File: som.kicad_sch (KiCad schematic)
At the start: 33 parts, among them M1 jetson-orin-nx/nano-module, U1 74LVC1T45GM

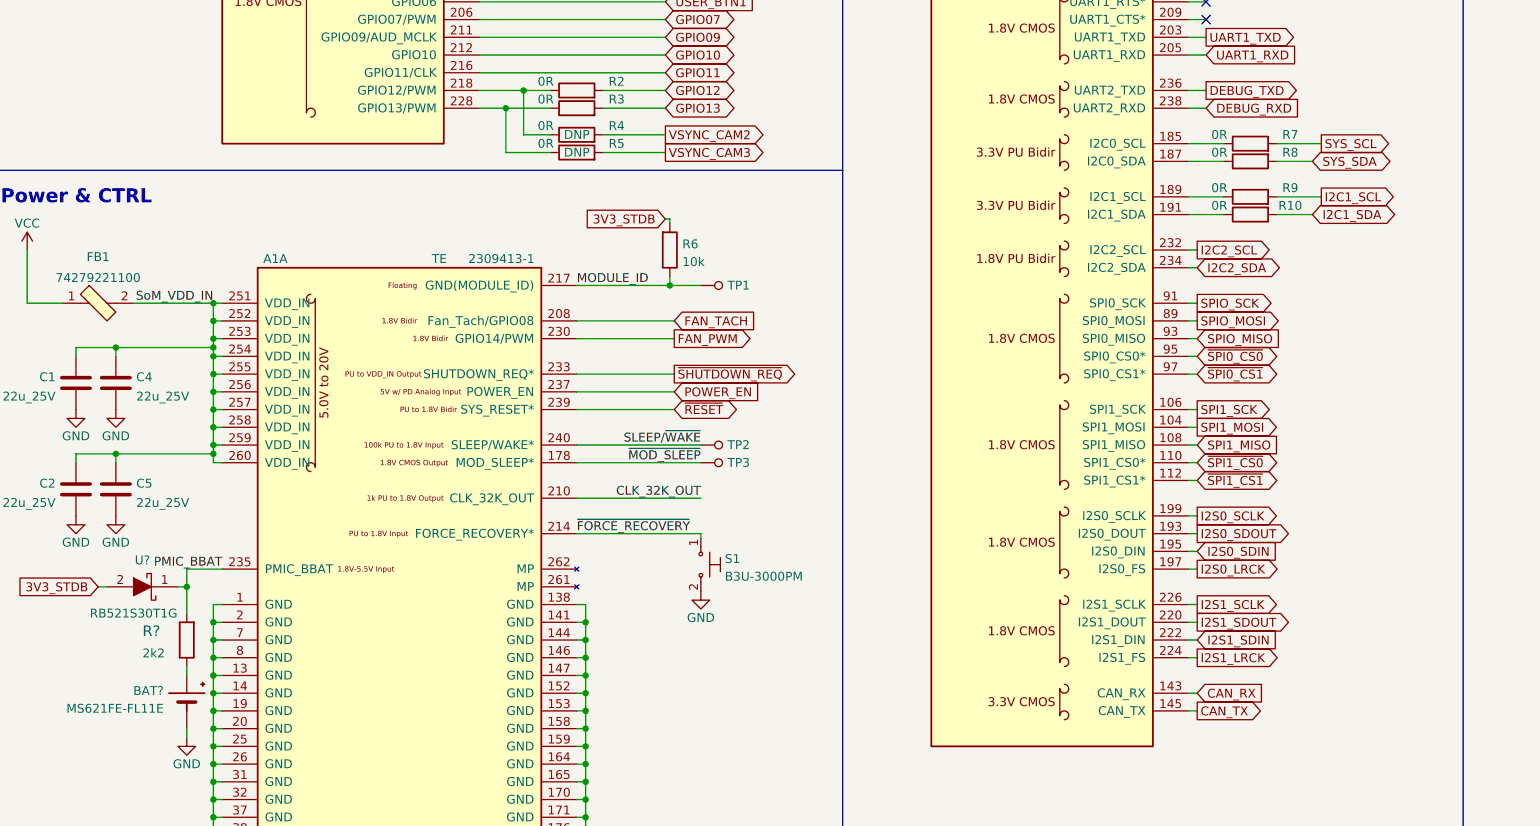
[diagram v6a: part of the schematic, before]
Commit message: Remove 0Rs from I2C pins near SoM
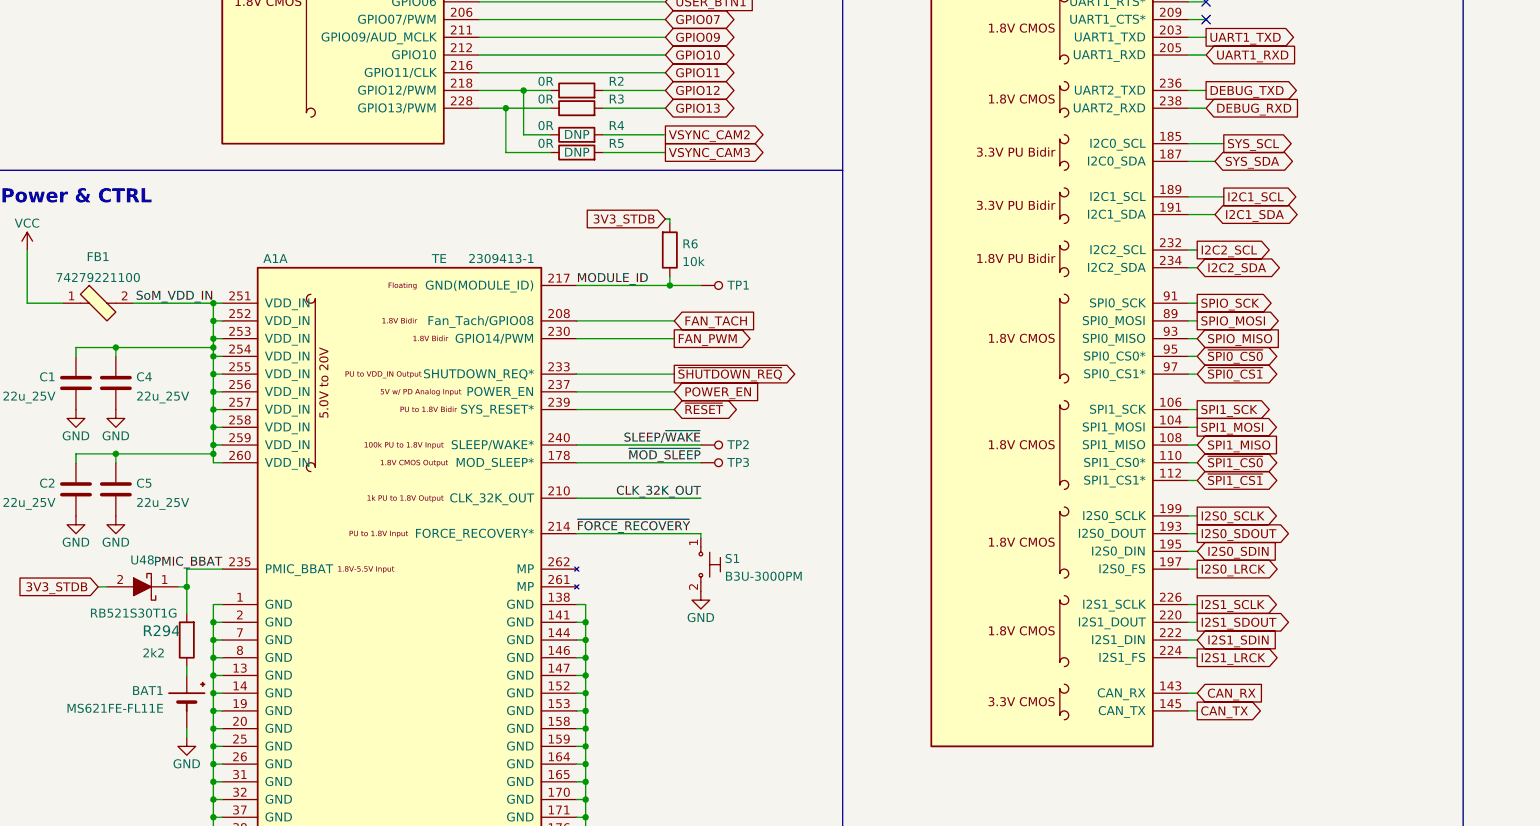
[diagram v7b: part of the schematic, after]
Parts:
- removed R10, R7, R8, R9: R_0R_0402, antmicro-footprints:0402-res, symbol antmicroResistors0402:R_0R_0402
- gave numbers to parts that had none: 3
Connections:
- net I2C1_SCL: now also A1.189 (I2C1_SCL)
- net I2C1_SDA: now also A1.191 (I2C1_SDA)
- net SYS_SCL: now also A1.185 (I2C0_SCL)
- net SYS_SDA: now also A1.187 (I2C0_SDA)
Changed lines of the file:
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@@
     (stroke (width 0) (type default) (color 0 0 0 0))
   )
-  (wire (pts (xy 207.01 73.66) (xy 201.93 73.66))
-    (stroke (width 0) (type default) (color 0 0 0 0))
-  )
   (wire (pts (xy 45.72 138.43) (xy 45.72 139.7))
     (stroke (width 0) (type default) (color 0 0 0 0))
@@
     (stroke (width 0) (type default) (color 0 0 0 0))
   )
-  (wire (pts (xy 194.31 66.04) (xy 189.23 66.04))
+  (wire (pts (xy 193.04 66.04) (xy 189.23 66.04))
     (stroke (width 0) (type default) (color 0 0 0 0))
   )
@@
     (stroke (width 0) (type default) (color 0 0 0 0))
   )
-  (wire (pts (xy 189.23 73.66) (xy 194.31 73.66))
+  (wire (pts (xy 189.23 73.66) (xy 193.04 73.66))
     (stroke (width 0) (type default) (color 0 0 0 0))
   )
@@
     (stroke (width 0) (type default) (color 0 0 0 0))
   )
-  (wire (pts (xy 208.28 63.5) (xy 201.93 63.5))
-    (stroke (width 0) (type default) (color 0 0 0 0))
-  )
   (wire (pts (xy 119.38 109.22) (xy 101.6 109.22))
     (stroke (width 0) (type default) (color 0 0 0 0))
@@
     (stroke (width 0) (type default) (color 0 0 0 0))
   )
-  (wire (pts (xy 207.01 66.04) (xy 201.93 66.04))
-    (stroke (width 0) (type default) (color 0 0 0 0))
-  )
   (wire (pts (xy 278.13 101.6) (xy 296.545 101.6))
     (stroke (width 0) (type default) (color 0 0 0 0))
@@
     (stroke (width 0) (type default) (color 0 0 0 0))
   )
-  (wire (pts (xy 194.31 63.5) (xy 189.23 63.5))
+  (wire (pts (xy 189.23 63.5) (xy 194.31 63.5))
     (stroke (width 0) (type default) (color 0 0 0 0))
   )
@@
     (stroke (width 0) (type default) (color 0 0 0 0))
   )
-  (wire (pts (xy 208.28 71.12) (xy 201.93 71.12))
-    (stroke (width 0) (type default) (color 0 0 0 0))
-  )
   (wire (pts (xy 190.5 93.98) (xy 189.23 93.98))
     (stroke (width 0) (type default) (color 0 0 0 0))
@@
     )
   )
-  (global_label "I2C1_SDA" (shape bidirectional) (at 207.01 73.66 0)
+  (global_label "I2C1_SDA" (shape bidirectional) (at 193.04 73.66 0)
     (effects (font (size 1.27 1.27)) (justify left))
-    (property "Intersheet References" "${INTERSHEET_REFS}" (id 0) (at 219.71 73.66 0)
+    (property "Intersheet References" "${INTERSHEET_REFS}" (id 0) (at 205.74 73.66 0)
       (effects (font (size 1.27 1.27)) (justify left))
     )
@@
     )
   )
-  (global_label "SYS_SDA" (shape bidirectional) (at 207.01 66.04 0)
+  (global_label "SYS_SDA" (shape bidirectional) (at 193.04 66.04 0)
     (effects (font (size 1.27 1.27)) (justify left))
-    (property "Intersheet References" "${INTERSHEET_REFS}" (id 0) (at 219.71 66.04 0)
+    (property "Intersheet References" "${INTERSHEET_REFS}" (id 0) (at 205.74 66.04 0)
       (effects (font (size 1.27 1.27)) (justify left))
     )
@@
     )
   )
-  (global_label "SYS_SCL" (shape output) (at 208.28 63.5 0)
+  (global_label "SYS_SCL" (shape output) (at 194.31 63.5 0)
     (effects (font (size 1.27 1.27)) (justify left))
-    (property "Intersheet References" "${INTERSHEET_REFS}" (id 0) (at 219.71 63.5 0)
+    (property "Intersheet References" "${INTERSHEET_REFS}" (id 0) (at 205.74 63.5 0)
       (effects (font (size 1.27 1.27)) (justify left))
     )
@@
     )
   )
-  (global_label "I2C1_SCL" (shape output) (at 208.28 71.12 0)
+  (global_label "I2C1_SCL" (shape output) (at 194.31 71.12 0)
     (effects (font (size 1.27 1.27)) (justify left))
-    (property "Intersheet References" "${INTERSHEET_REFS}" (id 0) (at 219.71 71.12 0)
+    (property "Intersheet References" "${INTERSHEET_REFS}" (id 0) (at 205.74 71.12 0)
       (effects (font (size 1.27 1.27)) (justify left))
     )
@@
     )
   )
-  (symbol (lib_id "antmicroResistors0402:R_0R_0402") (at 198.12 63.5 0) (unit 1)
-    (in_bom yes) (on_board yes)
-    (property "Reference" "R7" (id 0) (at 203.835 62.23 0))
-    (property "Value" "R_0R_0402" (id 1) (at 198.12 67.31 0)
-      (effects (font (size 1.27 1.27)) hide)
-    )
-    (property "Footprint" "antmicro-footprints:0402-res" (id 2) (at 203.2 58.42 0)
-      (effects (font (size 1.524 1.524)) (justify left) hide)
-    )
-    (property "Datasheet" "" (id 3) (at 198.12 63.5 0)
-      (effects (font (size 1.27 1.27)) hide)
-    )
-    (property "Manufacturer" "PANASONIC" (id 4) (at 203.2 53.34 0)
-      (effects (font (size 1.524 1.524)) (justify left) hide)
-    )
-    (property "MPN" "ERJ2GE0R00X" (id 5) (at 203.2 55.88 0)
-      (effects (font (size 1.524 1.524)) (justify left) hide)
-    )
-    (property "Val" "0R" (id 6) (at 193.675 62.23 0))
-    (pin "1")
-    (pin "2")
-  )
   (symbol (lib_id "power:+1V8") (at 24.765 237.49 0) (unit 1)
     (in_bom yes) (on_board yes)
@@
     (pin "1")
   )
-  (symbol (lib_id "antmicroResistors0402:R_0R_0402") (at 198.12 73.66 0) (mirror x) (unit 1)
-    (in_bom yes) (on_board yes)
-    (property "Reference" "R10" (id 0) (at 203.835 72.39 0))
-    (property "Value" "R_0R_0402" (id 1) (at 198.12 69.85 0)
-      (effects (font (size 1.27 1.27)) hide)
-    )
-    (property "Footprint" "antmicro-footprints:0402-res" (id 2) (at 203.2 78.74 0)
-      (effects (font (size 1.524 1.524)) (justify left) hide)
-    )
-    (property "Datasheet" "" (id 3) (at 198.12 73.66 0)
-      (effects (font (size 1.27 1.27)) hide)
-    )
-    (property "Manufacturer" "PANASONIC" (id 4) (at 203.2 83.82 0)
-      (effects (font (size 1.524 1.524)) (justify left) hide)
-    )
-    (property "MPN" "ERJ2GE0R00X" (id 5) (at 203.2 81.28 0)
-      (effects (font (size 1.524 1.524)) (justify left) hide)
-    )
-    (property "Val" "0R" (id 6) (at 193.675 72.39 0))
-    (pin "1")
-    (pin "2")
-  )
-  (symbol (lib_id "antmicroResistors0402:R_0R_0402") (at 198.12 71.12 0) (unit 1)
-    (in_bom yes) (on_board yes)
-    (property "Reference" "R9" (id 0) (at 203.835 69.85 0))
-    (property "Value" "R_0R_0402" (id 1) (at 198.12 74.93 0)
-      (effects (font (size 1.27 1.27)) hide)
-    )
-    (property "Footprint" "antmicro-footprints:0402-res" (id 2) (at 203.2 66.04 0)
-      (effects (font (size 1.524 1.524)) (justify left) hide)
-    )
-    (property "Datasheet" "" (id 3) (at 198.12 71.12 0)
-      (effects (font (size 1.27 1.27)) hide)
-    )
-    (property "Manufacturer" "PANASONIC" (id 4) (at 203.2 60.96 0)
-      (effects (font (size 1.524 1.524)) (justify left) hide)
-    )
-    (property "MPN" "ERJ2GE0R00X" (id 5) (at 203.2 63.5 0)
-      (effects (font (size 1.524 1.524)) (justify left) hide)
-    )
-    (property "Val" "0R" (id 6) (at 193.675 69.85 0))
-    (pin "1")
-    (pin "2")
-  )
   (symbol (lib_id "antmicroCapacitors0402:C_100n_0402") (at 24.765 241.3 0) (mirror y) (unit 1)
     (in_bom yes) (on_board yes) (fields_autoplaced)
@@
   (symbol (lib_id "antmicroDiodesRectifiersSingle:RB521S30T1G") (at 39.37 127 0) (unit 1)
     (in_bom yes) (on_board yes)
-    (property "Reference" "U?" (id 0) (at 39.37 123.19 0))
+    (property "Reference" "U48" (id 0) (at 39.37 123.19 0))
     (property "Value" "RB521S30T1G" (id 1) (at 38.1 130.81 0))
     (property "Footprint" "antmicro-footprints:SOD-523" (id 2) (at 41.91 134.62 0)
@@
     (pin "2")
   )
-  (symbol (lib_id "antmicroResistors0402:R_0R_0402") (at 198.12 66.04 0) (mirror x) (unit 1)
-    (in_bom yes) (on_board yes)
-    (property "Reference" "R8" (id 0) (at 203.835 64.77 0))
-    (property "Value" "R_0R_0402" (id 1) (at 198.12 62.23 0)
-      (effects (font (size 1.27 1.27)) hide)
-    )
-    (property "Footprint" "antmicro-footprints:0402-res" (id 2) (at 203.2 71.12 0)
-      (effects (font (size 1.524 1.524)) (justify left) hide)
-    )
-    (property "Datasheet" "" (id 3) (at 198.12 66.04 0)
-      (effects (font (size 1.27 1.27)) hide)
-    )
-    (property "Manufacturer" "PANASONIC" (id 4) (at 203.2 76.2 0)
-      (effects (font (size 1.524 1.524)) (justify left) hide)
-    )
-    (property "MPN" "ERJ2GE0R00X" (id 5) (at 203.2 73.66 0)
-      (effects (font (size 1.524 1.524)) (justify left) hide)
-    )
-    (property "Val" "0R" (id 6) (at 193.675 64.77 0))
-    (pin "1")
-    (pin "2")
-  )
   (symbol (lib_id "power:+3V3") (at 83.82 238.76 0) (unit 1)
     (in_bom yes) (on_board yes) (fields_autoplaced)
@@
   (symbol (lib_id "antmicroResistors0402:R_2k2_0402") (at 45.72 134.62 90) (unit 1)
     (in_bom yes) (on_board yes)
-    (property "Reference" "R?" (id 0) (at 39.37 133.35 90)
+    (property "Reference" "R294" (id 0) (at 39.37 133.35 90)
       (effects (font (size 1.524 1.524)) (justify right))
     )
@@
   (symbol (lib_id "power:GND") (at 45.72 148.59 0) (mirror y) (unit 1)
     (in_bom yes) (on_board yes) (fields_autoplaced)
-    (property "Reference" "#PWR?" (id 0) (at 45.72 154.94 0)
+    (property "Reference" "#PWR0313" (id 0) (at 45.72 154.94 0)
       (effects (font (size 1.27 1.27)) hide)
     )
@@
   (symbol (lib_id "antmicroBatteryHoldersClipsContacts:MS621FE-FL11E") (at 45.72 142.24 0) (mirror y) (unit 1)
     (in_bom yes) (on_board yes) (fields_autoplaced)
-    (property "Reference" "BAT?" (id 0) (at 42.4181 141.9133 0)
+    (property "Reference" "BAT1" (id 0) (at 42.4181 141.9133 0)
       (effects (font (size 1.27 1.27)) (justify left))
     )

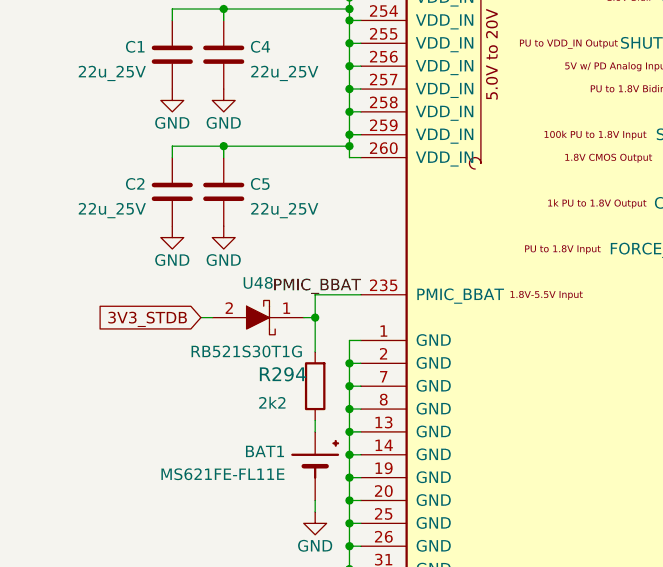
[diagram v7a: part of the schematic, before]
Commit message: Update RB521S30T1G symbol and footprint
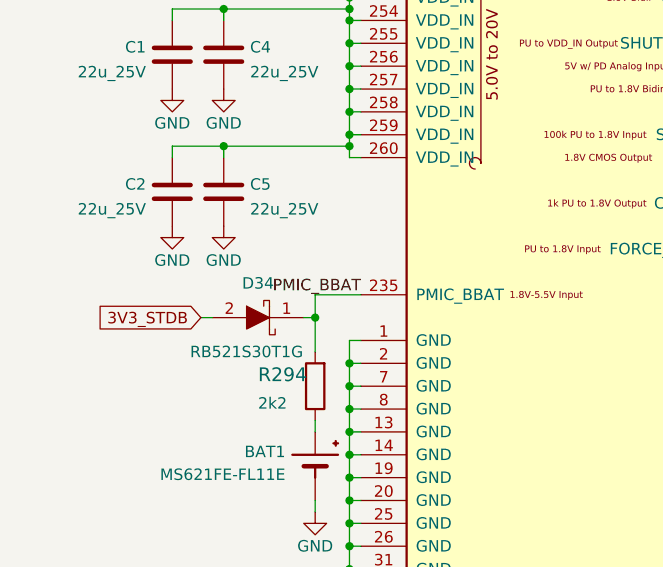
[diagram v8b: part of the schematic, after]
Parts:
- renumbered U48 to D34
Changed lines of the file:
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@@
   (symbol (lib_id "antmicroDiodesRectifiersSingle:RB521S30T1G") (at 39.37 127 0) (unit 1)
     (in_bom yes) (on_board yes)
-    (property "Reference" "U48" (id 0) (at 39.37 123.19 0))
+    (property "Reference" "D34" (id 0) (at 39.37 123.19 0))
     (property "Value" "RB521S30T1G" (id 1) (at 38.1 130.81 0))
     (property "Footprint" "antmicro-footprints:SOD-523" (id 2) (at 41.91 134.62 0)
